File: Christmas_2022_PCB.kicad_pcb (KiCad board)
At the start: 2 copper layers, 19 parts, among them J1 USB_A, SW1 SW_Push, SW2 SW_Push, U1 STM32F030K6Tx, U2 AMS1117-3.3

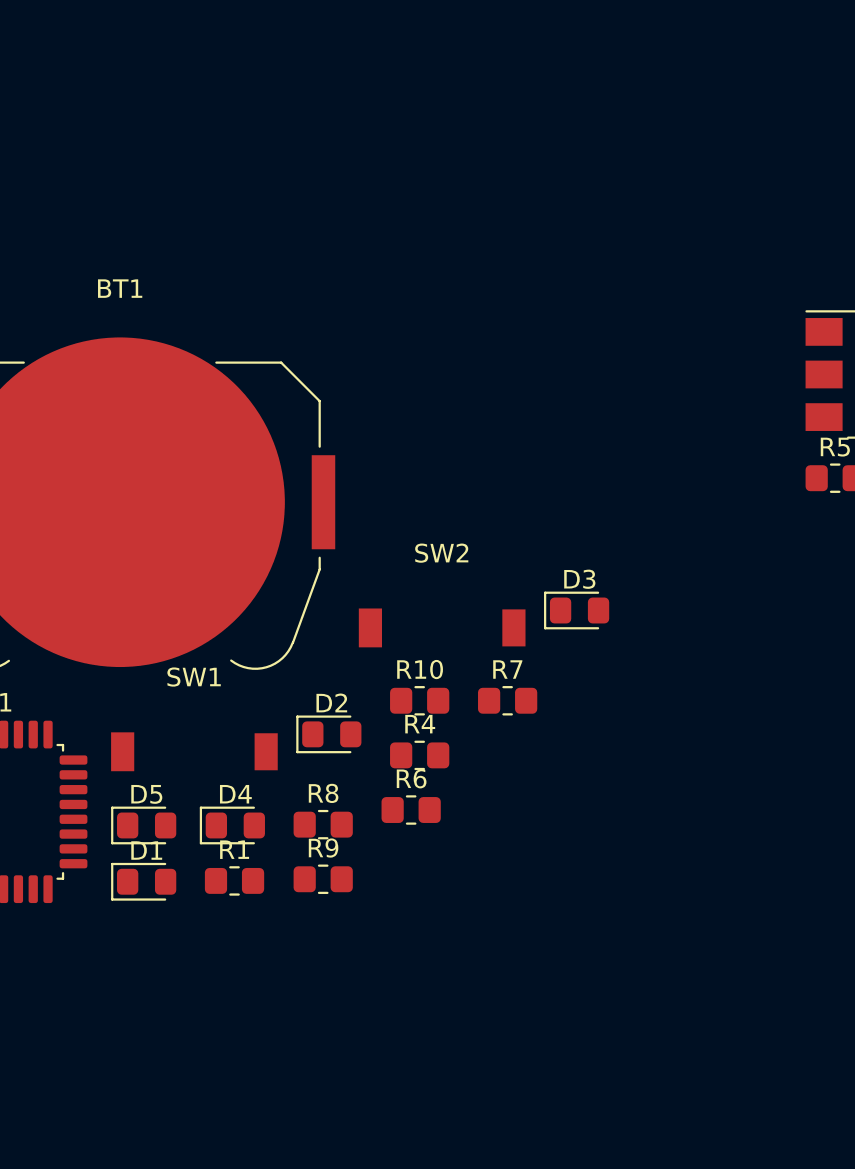
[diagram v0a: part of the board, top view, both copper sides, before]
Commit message: Added 3.3V slide switch
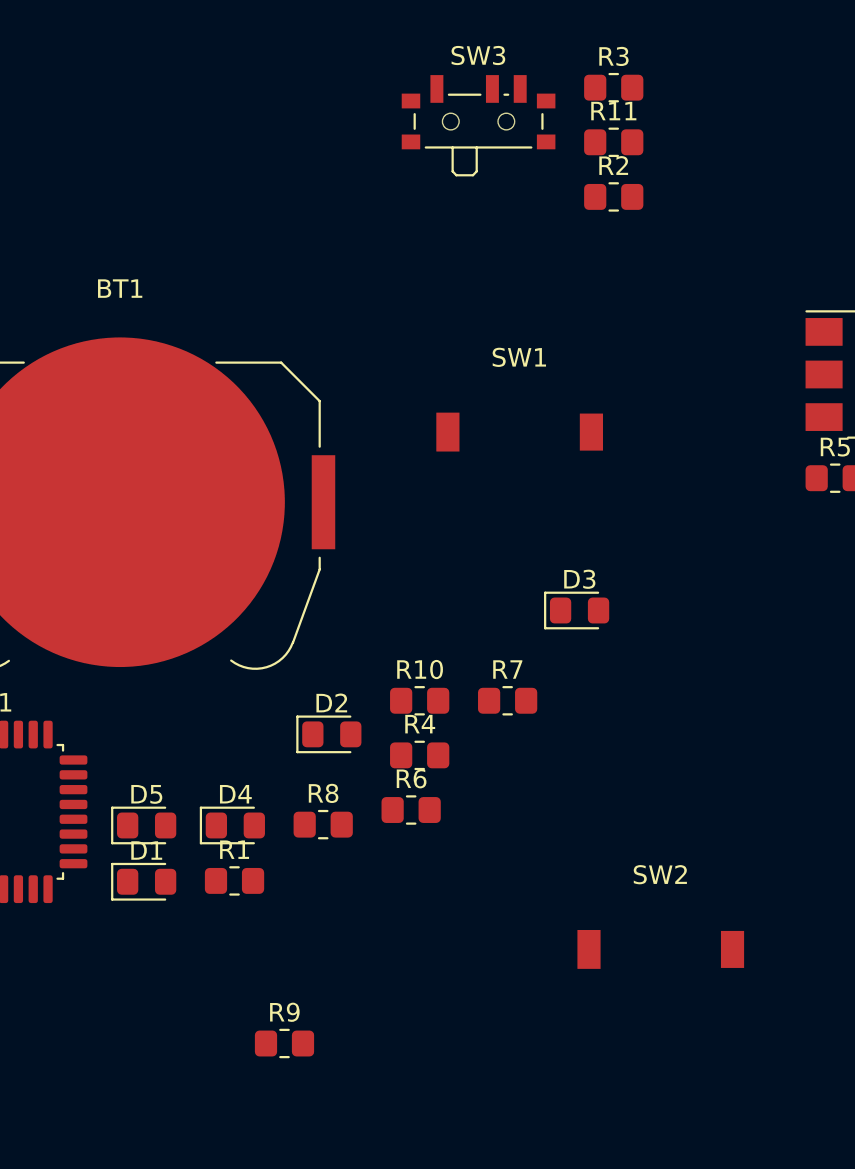
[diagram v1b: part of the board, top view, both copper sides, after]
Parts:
- added R11: 0, Resistor_SMD:R_0805_2012Metric_Pad1.20x1.40mm_HandSolder, F.Cu at (53.3, 19.9)
- added R2: R, Resistor_SMD:R_0805_2012Metric_Pad1.20x1.40mm_HandSolder, F.Cu at (53.3, 22.9)
- added R3: R, Resistor_SMD:R_0805_2012Metric_Pad1.20x1.40mm_HandSolder, F.Cu at (53.3, 17.0)
- added SW3: SW_SPDT, Button_Switch_SMD:SW_SPDT_PCM12, F.Cu at (46.0, 18.5)
- moved SW1 24.6 mm to (48.3, 35.6)
- moved SW2 21.0 mm to (55.9, 63.5)
- moved R9 9.11 mm to (35.6, 68.6)
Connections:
- BT1 pad 1: unconnected-(BT1-Pad1) -> /VBATT
- U2 pad 1: GND -> Net-(U2-Pad1)
- U2 pad 2: +3V3 -> /VREG

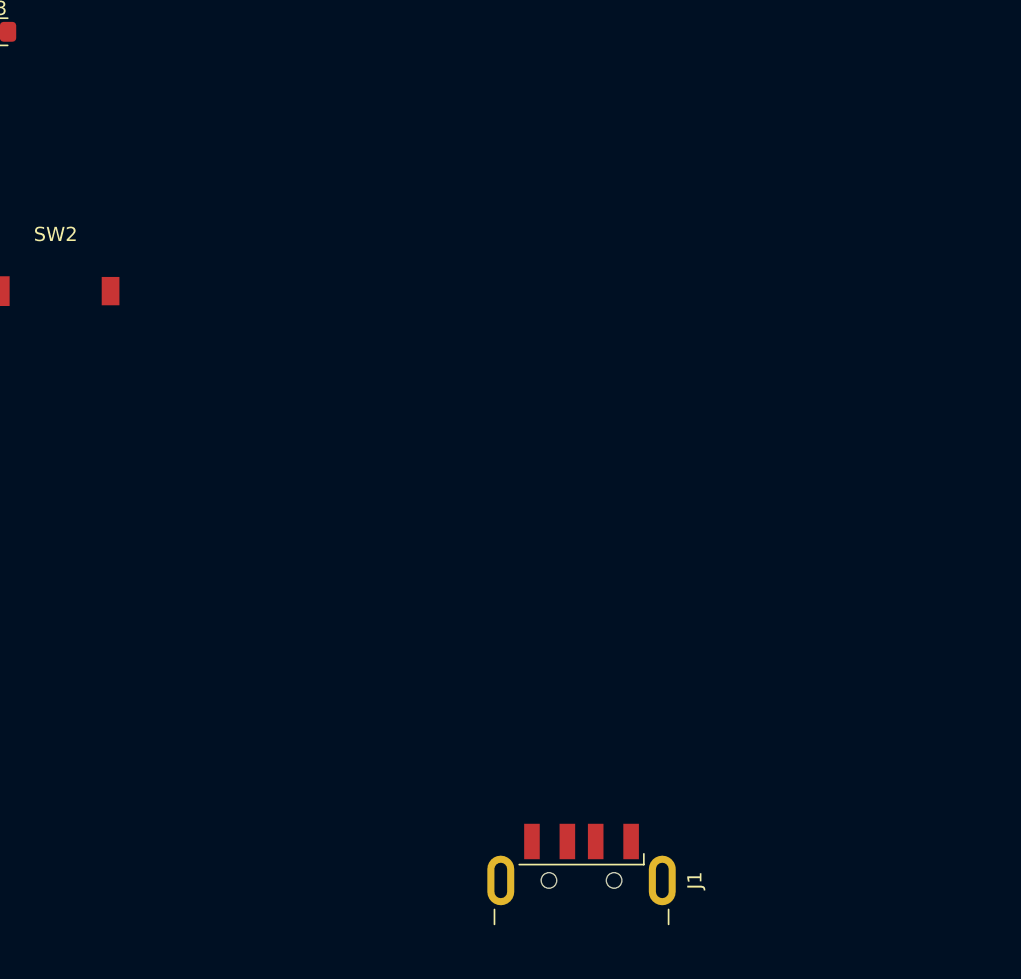
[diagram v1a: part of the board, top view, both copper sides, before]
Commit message: initial board outline added
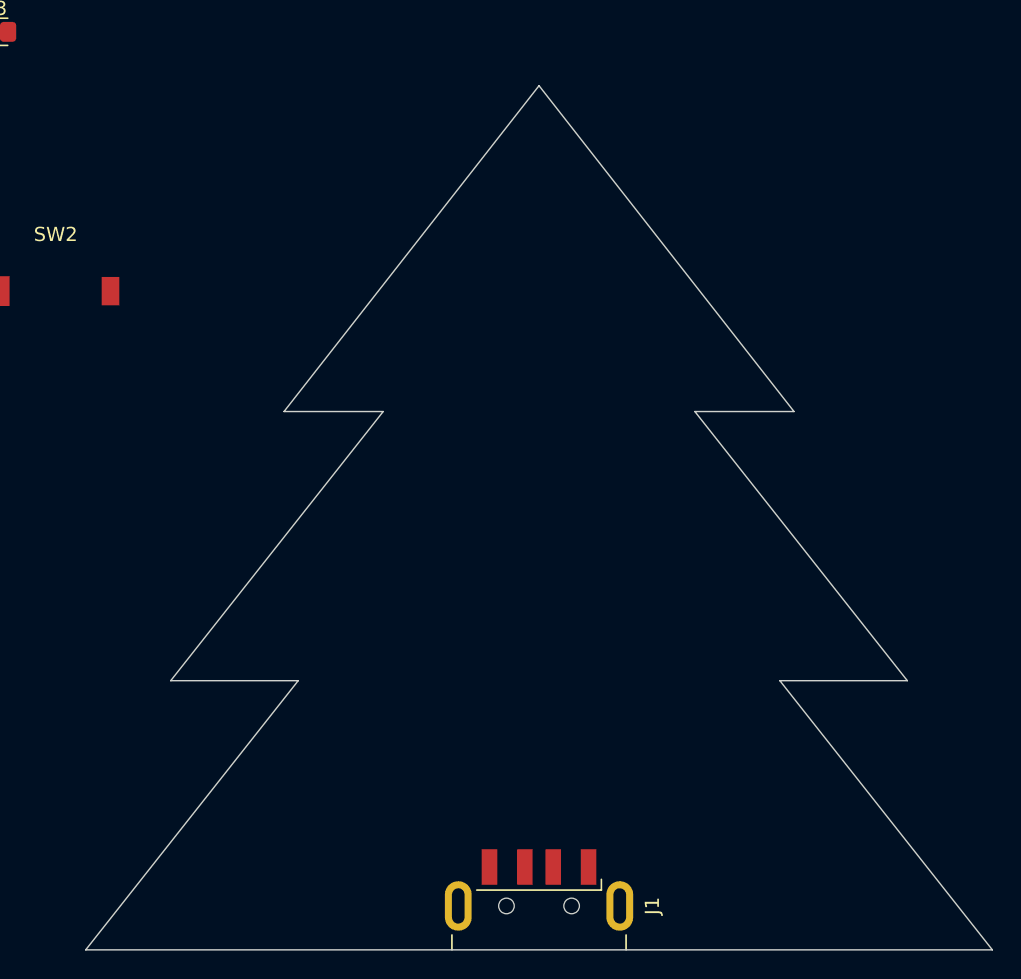
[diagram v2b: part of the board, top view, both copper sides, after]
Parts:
- moved J1 3.50 mm to (90.0, 113.8)
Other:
- board outline added: 64 x 61 mm

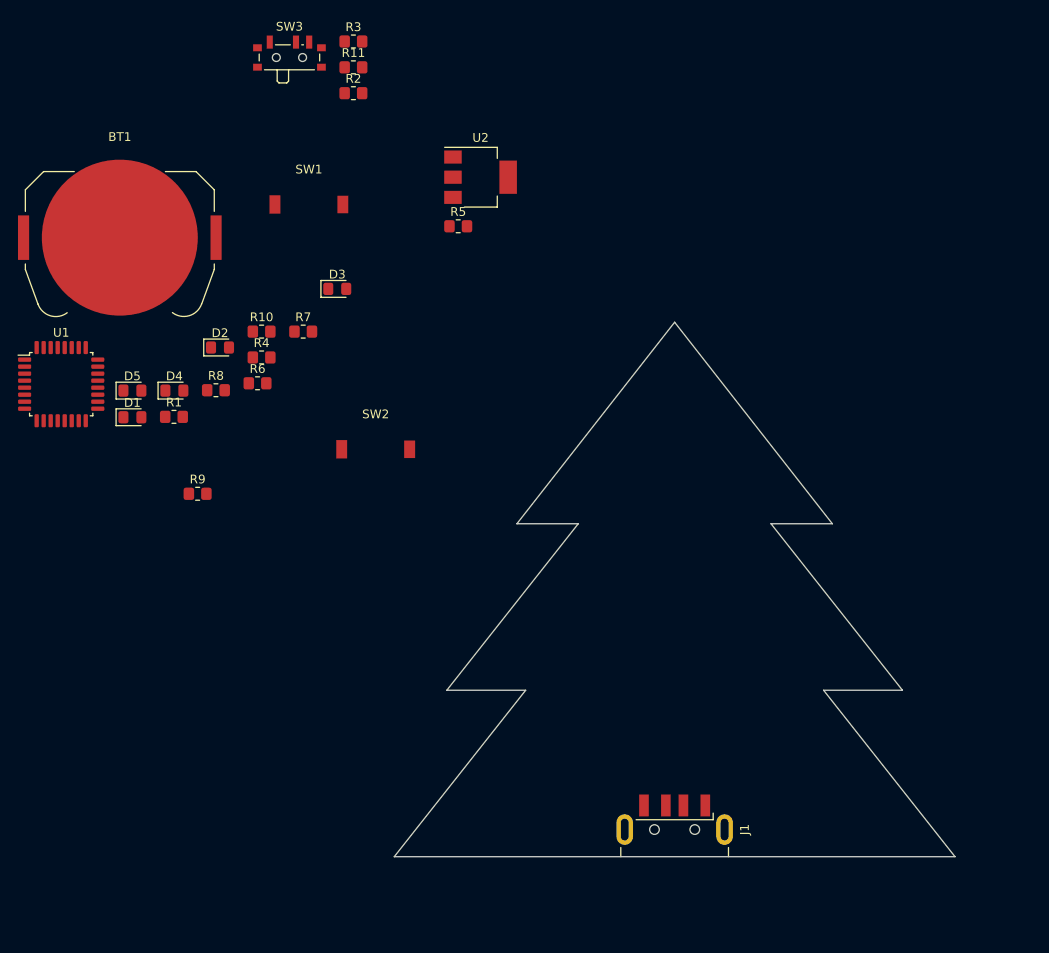
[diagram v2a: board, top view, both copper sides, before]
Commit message: began component placement
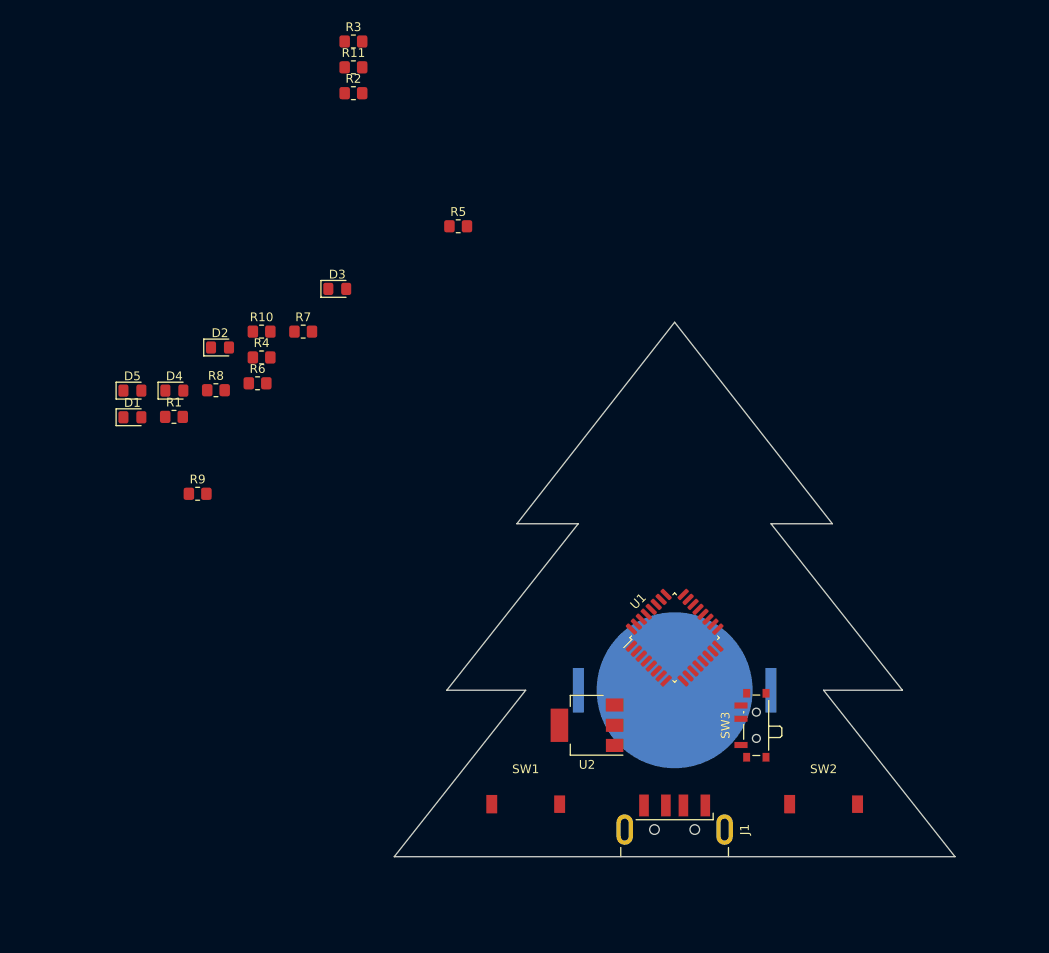
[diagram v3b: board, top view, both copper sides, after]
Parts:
- BT1: moved to B.Cu
- moved SW3 93.1 mm to (99.0, 95.0), turned to 90 degrees
- moved BT1 81.7 mm to (90.0, 91.0), turned to 180 degrees
- moved U1 75.8 mm to (90.0, 85.0), turned to 45 degrees
- moved SW1 72.8 mm to (73.0, 104.0)
- moved SW2 65.2 mm to (107.0, 104.0)
- moved U2 63.7 mm to (80.0, 95.0), turned to 180 degrees

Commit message: completed initial layout
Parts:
- added C1: C, Capacitor_SMD:C_0805_2012Metric_Pad1.18x1.45mm_HandSolder, F.Cu at (84.3, 84.8)
- added C2: C, Capacitor_SMD:C_0805_2012Metric_Pad1.18x1.45mm_HandSolder, F.Cu at (98.0, 81.0)
- added C3: C, Capacitor_SMD:C_0805_2012Metric_Pad1.18x1.45mm_HandSolder, F.Cu at (82.0, 81.0)
- added D6: LED, LED_SMD:LED_0805_2012Metric_Pad1.15x1.40mm_HandSolder, F.Cu at (90.0, 61.0)
- added D7: LED, LED_SMD:LED_0805_2012Metric_Pad1.15x1.40mm_HandSolder, F.Cu at (103.0, 70.0)
- added R12: R, Resistor_SMD:R_0805_2012Metric_Pad1.20x1.40mm_HandSolder, F.Cu at (90.0, 65.0)
- added R13: R, Resistor_SMD:R_0805_2012Metric_Pad1.20x1.40mm_HandSolder, F.Cu at (98.0, 70.0)
- added REF**: MountingHole_3mm, MountingHole:MountingHole_3mm, F.Cu at (90.0, 55.0)
- moved D3 90.7 mm to (117.0, 108.0)
- moved D5 88.9 mm to (111.0, 89.0), turned to 180 degrees
- moved R3 86.8 mm to (87.0, 97.0), turned to 90 degrees
- moved R7 86.6 mm to (112.0, 108.0)
- moved R11 85.3 mm to (92.1, 95.9), turned to 180 degrees
- moved R2 77.8 mm to (87.0, 93.0), turned to -90 degrees
- moved R8 77.4 mm to (99.0, 104.0)
- moved R10 74.2 mm to (106.0, 89.0)
- moved R4 63.7 mm to (81.0, 104.0), turned to 180 degrees
- moved D4 59.4 mm to (63.0, 108.0)
- moved R1 51.7 mm to (82.0, 76.0), turned to 180 degrees
- moved R9 51.1 mm to (68.0, 108.0)
- moved D1 49.9 mm to (77.0, 70.0)
- moved D2 48.3 mm to (69.0, 89.0)
- moved R6 45.7 mm to (74.0, 89.0), turned to 180 degrees
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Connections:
- SW1 pad 2: GND -> /BUT_LEFT
- SW2 pad 2: GND -> /BUT_RIGHT
- U1 pad 20: unconnected-(U1-Pad20) -> /LED6
- U1 pad 21: unconnected-(U1-Pad21) -> /LED7

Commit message: began routing
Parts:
- added J2: SOP8_test_point, Library:sop_8_test_pad, F.Cu at (98.5, 63.2)
- added J3: SOP8_test_point, Library:sop_8_test_pad, B.Cu at (98.5, 63.2)
- moved R1 14.6 mm to (96.0, 80.0), turned to 0 degrees
- moved C3 5.00 mm to (82.0, 76.0), turned to 180 degrees
- moved C2 5.00 mm to (98.0, 76.0)
- moved U1 5.00 mm to (90.0, 75.0)
- moved C1 4.81 mm to (84.0, 80.0)
- moved R4 1.80 mm to (81.0, 102.2)
- moved R8 1.80 mm to (99.0, 102.2)
- moved SW1 1.80 mm to (73.0, 102.2)
- moved SW2 1.80 mm to (107.0, 102.2)
- turned D3 to 180 degrees
- turned R3 to -90 degrees
- turned R5 to 180 degrees
- turned R9 to 180 degrees
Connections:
- U1 pad 4: unconnected-(U1-Pad4) -> /NRST
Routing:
- net /LED4: track 0.00 -> 52.4 mm, vias 0 -> 2
- net /LED3: track 0.00 -> 39.8 mm
- net /BUT_RIGHT: track 0.00 -> 38.3 mm
- net /VBATT: track 0.00 -> 38.3 mm, vias 0 -> 2
- net /BUT_LEFT: track 0.00 -> 34.7 mm
- net GND: track 0.00 -> 33.9 mm, vias 0 -> 15
- net /LED2: track 0.00 -> 28.2 mm, vias 0 -> 2
- net /LED5: track 0.00 -> 24.7 mm
- net /NRST: track 0.00 -> 23.7 mm, vias 0 -> 1
- net Net-(J1-Pad1): track 0.00 -> 22.5 mm, vias 0 -> 2
- net /VREG: track 0.00 -> 22.3 mm
- net /LED1: track 0.00 -> 13.5 mm, vias 0 -> 2
- net /SWDIO: track 0.00 -> 10.5 mm
- net /SWCLK: track 0.00 -> 10.4 mm
- net /LED6: track 0.00 -> 8.80 mm, vias 0 -> 2
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- added copper zone on F.Cu, net +3V3
- added copper zone on B.Cu, net GND
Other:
- board size 64 x 61 mm -> 61.4 x 60.5 mm
- board text added: "merry christmas"
